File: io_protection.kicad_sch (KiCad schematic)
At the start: 0 parts

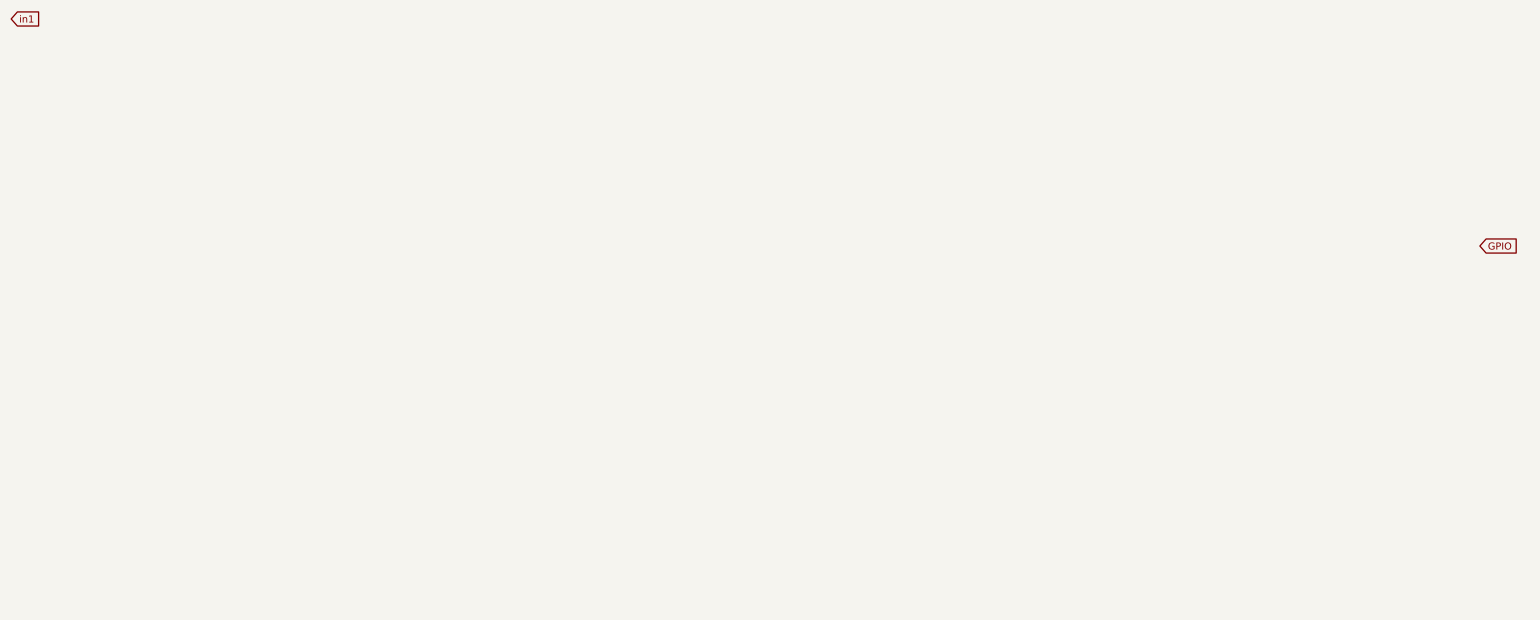
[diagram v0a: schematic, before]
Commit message: added i2c to io_protection
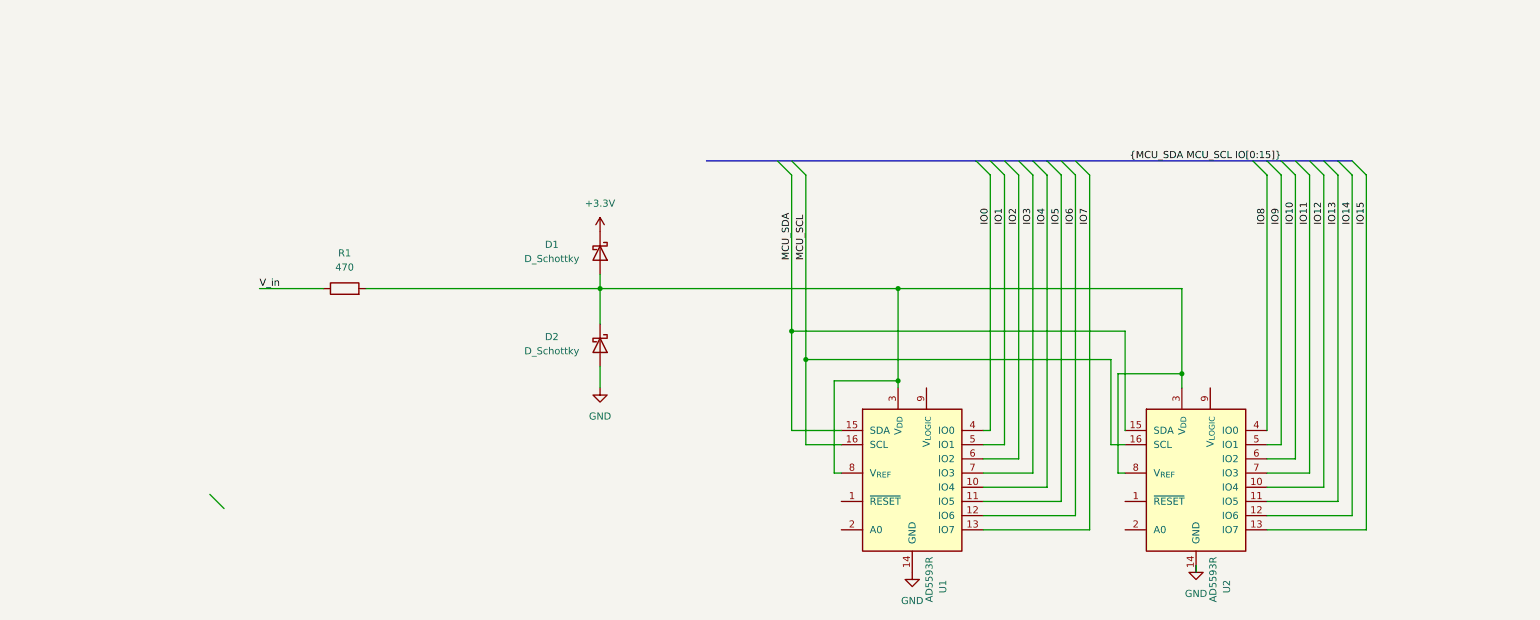
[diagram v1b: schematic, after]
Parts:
- added D1, D2: D_Schottky, symbol Device:D_Schottky
- added R1: 470, symbol Device:R
- added U1, U2: AD5593R, Package_SO:TSSOP-16_4.4x5mm_P0.65mm, symbol Analog:AD5593R
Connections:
- new net: D1.2 (A), D2.1 (K), R1.2, U1.3 (V_{DD}), U1.8 (V_{REF}), U2.3 (V_{DD}), U2.8 (V_{REF})
- new net +3.3V: D1.1 (K)
- new net GND: D2.2 (A), U1.14 (GND), U2.14 (GND)
- new net IO0: U1.4 (IO0)
- new net IO1: U1.5 (IO1)
- new net IO10: U2.6 (IO2)
- new net IO11: U2.7 (IO3)
- new net IO12: U2.10 (IO4)
- new net IO13: U2.11 (IO5)
- new net IO14: U2.12 (IO6)
- new net IO15: U2.13 (IO7)
- new net IO2: U1.6 (IO2)
- new net IO3: U1.7 (IO3)
- new net IO4: U1.10 (IO4)
- new net IO5: U1.11 (IO5)
- new net IO6: U1.12 (IO6)
- new net IO7: U1.13 (IO7)
- new net IO8: U2.4 (IO0)
- new net IO9: U2.5 (IO1)
- new net MCU_SCL: U1.16 (SCL), U2.16 (SCL)
- new net MCU_SDA: U1.15 (SDA), U2.15 (SDA)
- new net V_in: R1.1

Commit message: added i2c buffer + wired a0 to gnd
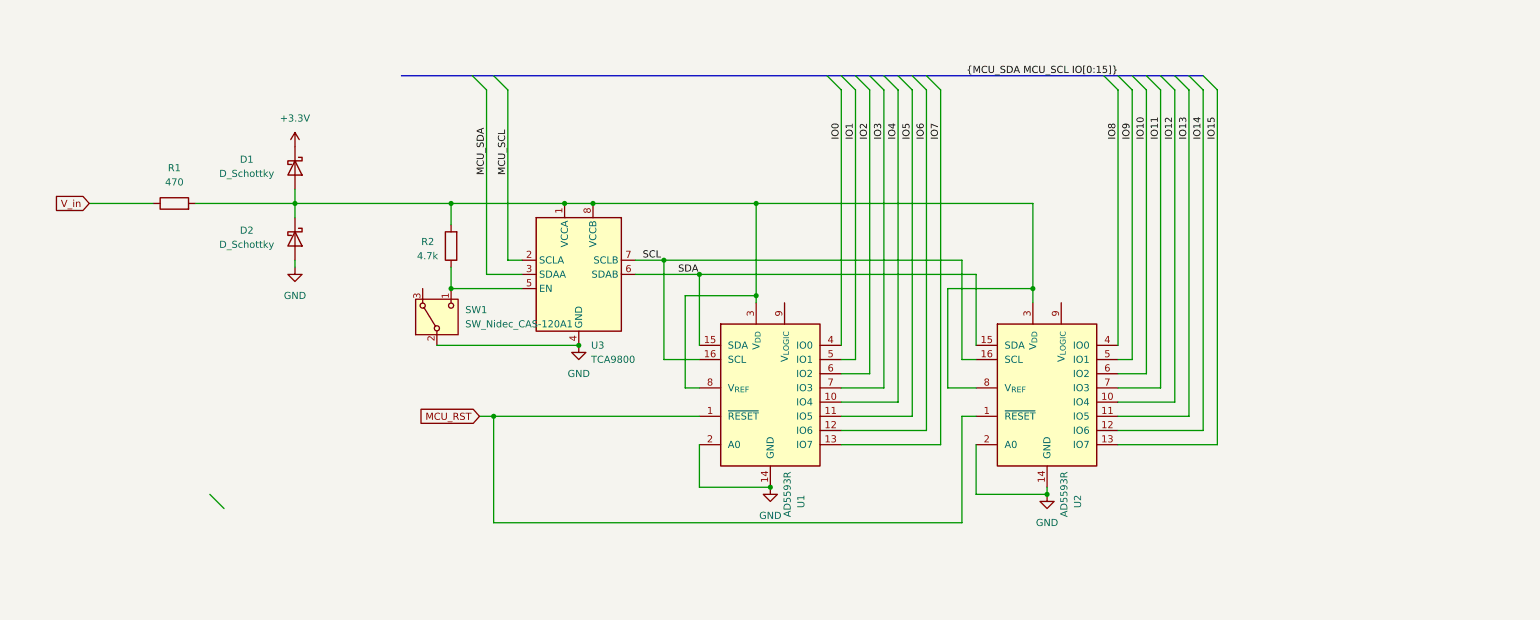
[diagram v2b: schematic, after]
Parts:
- added R2: 4.7k, symbol Device:R
- added SW1: SW_Nidec_CAS-120A1, Button_Switch_SMD:Nidec_Copal_CAS-120A, symbol Switch:SW_Nidec_CAS-120A1
- added U3: TCA9800, Package_SO:VSSOP-8_3x3mm_P0.65mm, symbol Interface:TCA9800
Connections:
- net GND: now also U1.2 (A0), U2.2 (A0), SW1.2 (B), U3.4 (GND)
- net MCU_SCL: now also U3.2 (SCLA); no longer U1.16 (SCL), U2.16 (SCL)
- net MCU_SDA: now also U3.3 (SDAA); no longer U1.15 (SDA), U2.15 (SDA)
- net at D1.2 (A), D2.1 (K), R1.2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: now also R2.2, U3.1 (VCCA), U3.8 (VCCB)
- net MCU_RST: now reaches U2.1 (~{RESET})
- net MCU_RST: now also U1.1 (~{RESET})
- new net: R2.1, SW1.1 (C), U3.5 (EN)
- new net SCL: U1.16 (SCL), U2.16 (SCL), U3.7 (SCLB)
- new net SDA: U1.15 (SDA), U2.15 (SDA), U3.6 (SDAB)
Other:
- moved on the sheet: D1, D2, R1, U1, U2
